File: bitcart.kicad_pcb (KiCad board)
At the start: 4 copper layers, 110 x 100 mm, 129 parts, among them J1 USB_OTG, J10 Conn_02x03_Odd_Even, J12 0455580003, J13 Hashboard0, J14 Hashboard1, J15 Hashboard2, J16 0353180420, J17 0353180420, J18 0353180420, J19 0353180420, J2 690-008-221-904, J3 61900411021, J4 61900411021, J5 61900411021, J6 61900411021, J7 Conn_01x22, J8 Conn_01x02, J9 THD-20-R, Q1 DMP3013SFV-7, U1 FSUSB42MUX, U10 PCA9546ARGVR, U2 USB2514B-I/M2, U3 TPD4EUSB30, U4 AP22653W6, U5 EMC2305-1-AP-TR, U6 74LVC1G07SE-7, U7 MagJack-A70-112-331N126, U9 AP64501SP-13, Y1 24MHz

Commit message: more routing
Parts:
- moved TP2 65.6 mm to (110.0, 69.5)
- moved TP1 64.2 mm to (106.3, 71.1)
- moved TP6 54.1 mm to (160.5, 64.3)
- moved TP7 44.6 mm to (167.5, 78.6)
- moved C15 22.8 mm to (162.2, 114.9)
- moved R17 21.9 mm to (119.0, 130.0)
- moved C16 18.5 mm to (162.2, 117.0), turned to 180 degrees
- moved R18 14.5 mm to (137.6, 130.0)
- moved R2 2.81 mm to (148.9, 114.9), turned to 90 degrees
- moved C5 1.45 mm to (150.6, 113.2), turned to 180 degrees
- moved C13 1.12 mm to (165.6, 118.9)
- moved R1 0.83 mm to (150.1, 114.9)
- moved C11 0.78 mm to (159.9, 106.2)
- moved C14 0.60 mm to (162.2, 119.0)
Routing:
- net /5V: track 16.1 -> 143.3 mm, vias 1 -> 31
- net /nEXTRST: track 10.3 -> 94.7 mm
- net /CM4_GPIO ( Ethernet, GPIO, SDCARD)/nPWR_LED: track 8.17 -> 85.7 mm, vias 1 -> 4
- net /CM4_GPIO ( Ethernet, GPIO, SDCARD)/nRPIBOOT: track 9.04 -> 79.3 mm, vias 2 -> 3
- net Net-(Module1A-PI_nLED_Activity): track 9.39 -> 75.5 mm, vias 1 -> 2
- net /CM4_GPIO ( Ethernet, GPIO, SDCARD)/ETH_LEDY: track 10.3 -> 66.1 mm
- net /CM4_GPIO ( Ethernet, GPIO, SDCARD)/ETH_LEDG: track 11.2 -> 63.8 mm, vias 0 -> 2
- net GND: track 142.8 -> 116.8 mm, vias 166 -> 155
- net /USB2-HUB/VBUS: track 25.8 -> 0.00 mm
- net /USB2-HUB/PWR1: track 9.04 -> 33.1 mm, vias 0 -> 2
- net /USB2-HUB/nOCS1: track 16.4 -> 34.9 mm
- net Net-(J1-VBUS): track 0.75 -> 19.1 mm, vias 1 -> 2
- net (no net): track 64.1 -> 46.6 mm
- net /CM4_HighSpeed/USBOTG_ID: track 18.9 -> 32.6 mm, vias 0 -> 2
- net /3V3: track 43.4 -> 30.5 mm, vias 14 -> 13
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- added copper zone on In2.Cu, net /3V3
- added copper zone on F.Cu, net /USB2-HUB/VBUS

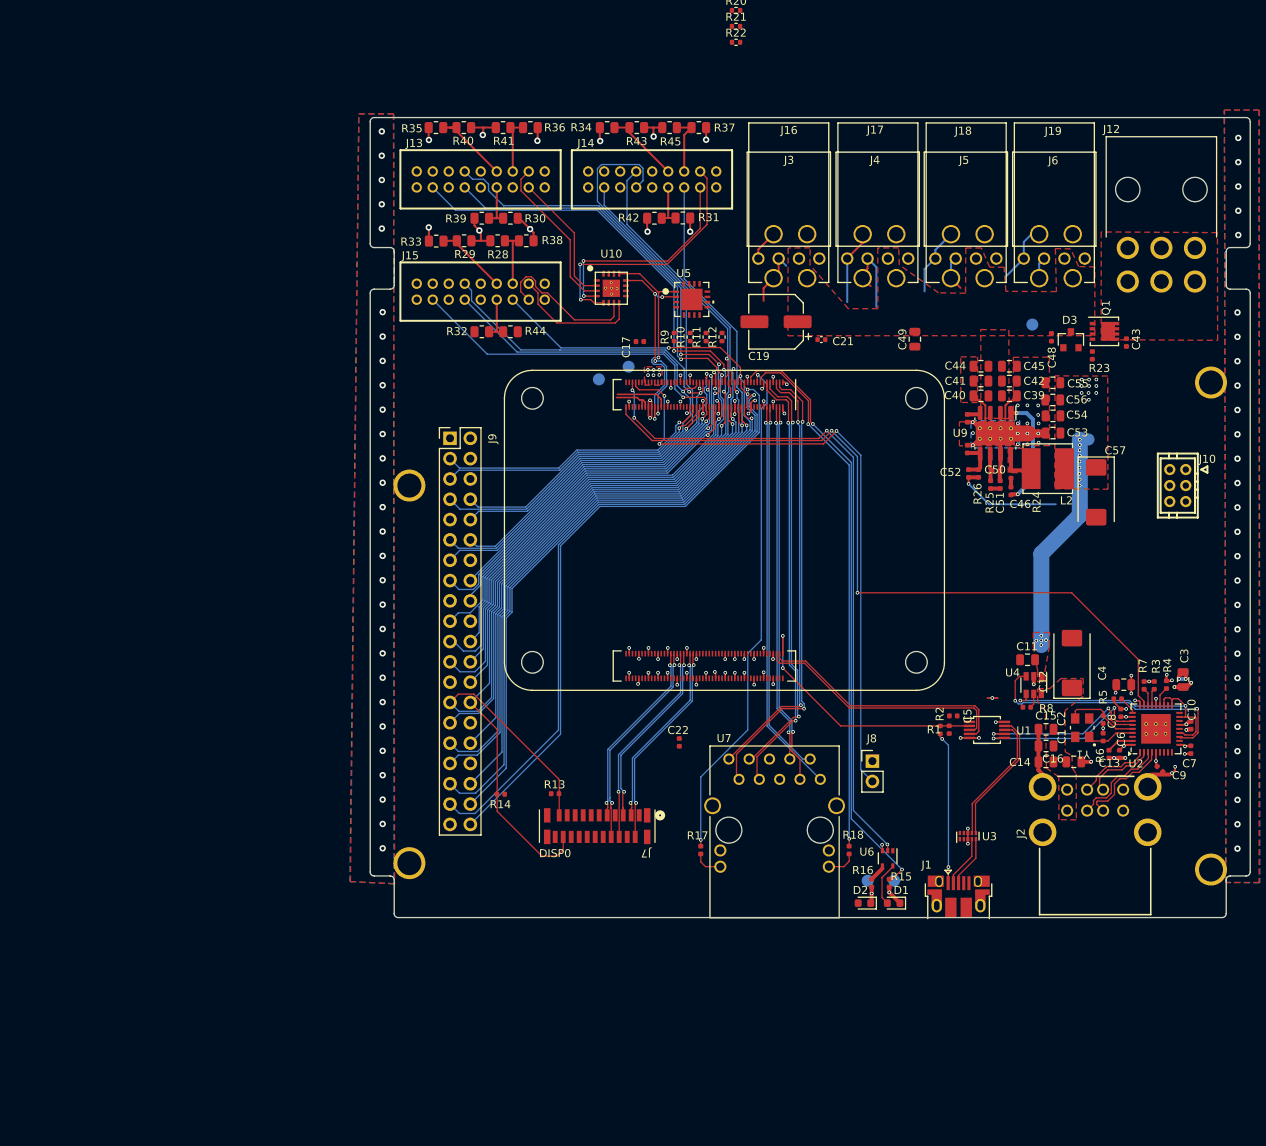
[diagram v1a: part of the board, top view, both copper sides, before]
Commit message: added more USB ports.. placing
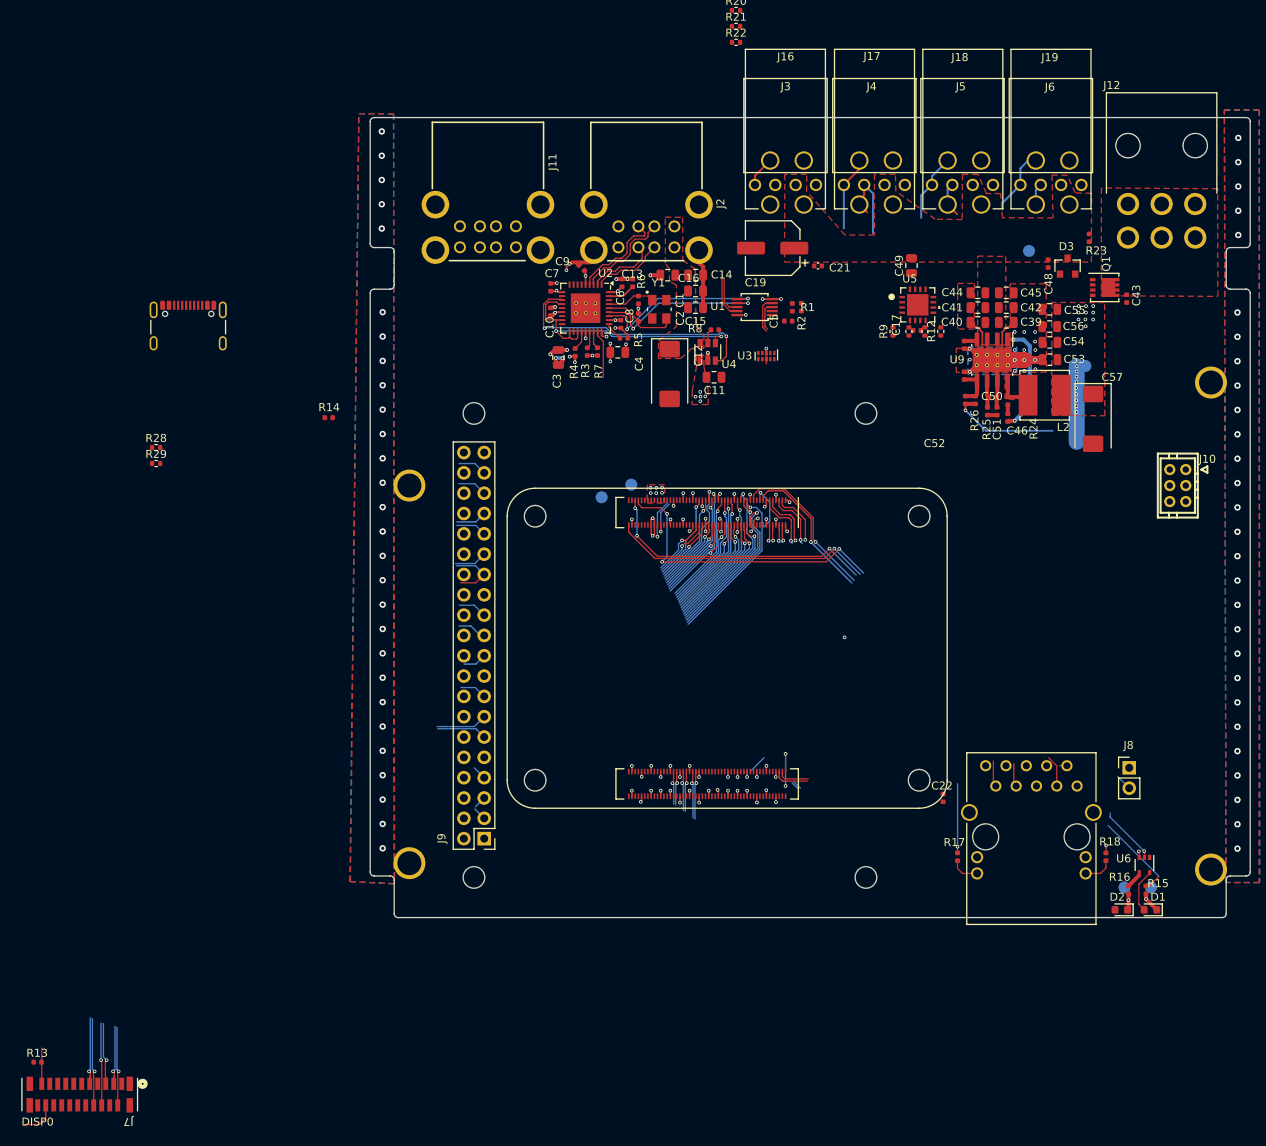
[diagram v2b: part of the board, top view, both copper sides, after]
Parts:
- removed J1: USB_OTG, CM4IO:USB_Micro-B_EDAC_UCON00686
- removed J14: Hashboard1, bitcart:CONN-TH_X2026WV-2-09D-46SN
- removed J15: Hashboard2, bitcart:CONN-TH_X2026WV-2-09D-46SN
- removed R30, R31, R32, R33, R34, R35, R36, R37, R38, R39, R40, R41, R42, R43, R44, R45: 4.7K, Resistor_SMD:R_0805_2012Metric
- removed U10: PCA9546ARGVR, bitcart:QFN-16_EP_4x4_Pitch0.65mm
- added H5: MountingHole, MountingHole:MountingHole_2.7mm_M2.5, F.Cu at (90.7, 75.4)
- added H6: MountingHole, MountingHole:MountingHole_2.7mm_M2.5, F.Cu at (90.7, 133.4)
- added H7: MountingHole, MountingHole:MountingHole_2.7mm_M2.5, F.Cu at (139.7, 133.4)
- added H8: MountingHole, MountingHole:MountingHole_2.7mm_M2.5, F.Cu at (139.7, 75.4)
- added J11: 690-008-221-904, CM4IO:MOLEX_USB_67298-4090, F.Cu at (92.4, 49.3)
- J13: value Hashboard0 -> USB_C_Receptacle_USB2.0; footprint bitcart:CONN-TH_X2026WV-2-09D-46SN -> bitcart:USB_C_Receptacle_GCT_USB4105-xx-A_16P_TopMnt_Horizontal
- R28, R29: value 4.7K -> 5.1k; footprint Resistor_SMD:R_0805_2012Metric -> Resistor_SMD:R_0402_1005Metric
- moved C7 98.7 mm to (100.3, 59.6), turned to 90 degrees
- moved J2 96.4 mm to (112.2, 49.3), turned to 180 degrees
- moved C9 95.7 mm to (104.1, 57.2), turned to 135 degrees
- moved C10 95.3 mm to (100.2, 62.7), turned to 90 degrees
- moved U2 88.6 mm to (104.6, 62.2), turned to -90 degrees
- moved C3 87.9 mm to (101.2, 68.4), turned to -90 degrees
- moved C6 85.7 mm to (109.2, 59.1), turned to 90 degrees
- moved R4 84.8 mm to (103.3, 67.8), turned to -90 degrees
- moved R6 83.8 mm to (110.5, 59.1), turned to -90 degrees
- moved R3 82.2 mm to (104.8, 67.7), turned to -90 degrees
- moved R7 80.1 mm to (106.1, 67.7), turned to -90 degrees
- moved C1 79.8 mm to (111.2, 61.2), turned to -90 degrees
- moved C13 79.2 mm to (114.9, 58.1), turned to 180 degrees
- moved C8 79.2 mm to (109.0, 64.2), turned to -90 degrees
- moved C2 76.8 mm to (111.2, 63.4), turned to 90 degrees
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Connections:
- R2 pad 1: Net-(J1-VBUS) -> Net-(J13-VBUS-PadA4B9)
- R28 pad 1: /hashboards/A0-1 -> GND
- R28 pad 2: GND -> Net-(J13-CC1)
- R29 pad 1: /hashboards/A2-1 -> GND
- R29 pad 2: GND -> Net-(J13-CC2)
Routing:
- net /CM4_GPIO ( Ethernet, GPIO, SDCARD)/GPIO11: track 112.4 -> 16.2 mm, vias 4 -> 1
- net /CM4_GPIO ( Ethernet, GPIO, SDCARD)/GPIO9: track 107.6 -> 15.0 mm, vias 3 -> 1
- net /CM4_GPIO ( Ethernet, GPIO, SDCARD)/GPIO8: track 104.3 -> 15.5 mm, vias 2 -> 1
- net /CM4_GPIO ( Ethernet, GPIO, SDCARD)/GPIO16: track 106.4 -> 20.2 mm, vias 2 -> 1
- net /CM4_GPIO ( Ethernet, GPIO, SDCARD)/GPIO6: track 99.9 -> 18.2 mm
- net /CM4_GPIO ( Ethernet, GPIO, SDCARD)/GPIO5: track 99.4 -> 17.7 mm
- net /CM4_GPIO ( Ethernet, GPIO, SDCARD)/GPIO7: track 91.2 -> 15.3 mm
- net /CM4_GPIO ( Ethernet, GPIO, SDCARD)/GPIO4: track 84.4 -> 9.95 mm
- net /CM4_GPIO ( Ethernet, GPIO, SDCARD)/GPIO17: track 83.2 -> 15.5 mm, vias 2 -> 1
- net /CM4_GPIO ( Ethernet, GPIO, SDCARD)/ID_SC: track 87.4 -> 20.3 mm
- net /CM4_GPIO ( Ethernet, GPIO, SDCARD)/GPIO15: track 76.0 -> 11.7 mm, vias 2 -> 1
- net /CM4_GPIO ( Ethernet, GPIO, SDCARD)/GPIO14: track 72.6 -> 10.9 mm
- net /CM4_GPIO ( Ethernet, GPIO, SDCARD)/ID_SD: track 84.8 -> 25.1 mm
- net /CM4_GPIO ( Ethernet, GPIO, SDCARD)/GPIO21: track 77.8 -> 20.6 mm
- net /CM4_GPIO ( Ethernet, GPIO, SDCARD)/GPIO26: track 79.5 -> 23.7 mm
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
